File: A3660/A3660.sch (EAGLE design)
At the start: 130 parts, among them CN100 KEL8817-200-170S-F, J400 1X3PIN, U100 OSCILLATOR, U101 74F1803, U102 MC68040/68060, U103 DELAYLINE, U104 7407, U105 74F04, U200 74FCT373ASO, U201 74FCT374ASO, U202 74F32, U203 GAL16V8, U204 GAL22V10, U205 GAL22V10, U206 74F139, U207 GAL22V10, U208 GAL16V8, U209 GAL22V10, U211 GAL22V10, U212 74F257, U213 GAL22V10, U214 74FCT543A, U215 74FCT543A, U216 74FCT543A, U217 74FCT543A, U218 74FCT543A, U219 74FCT543A, U220 74FCT543A, U221 74FCT543A, U222 74FCT543A, U400 GAL22V10, U401 GAL16V8, U402 74FCT244A, U500 74F257

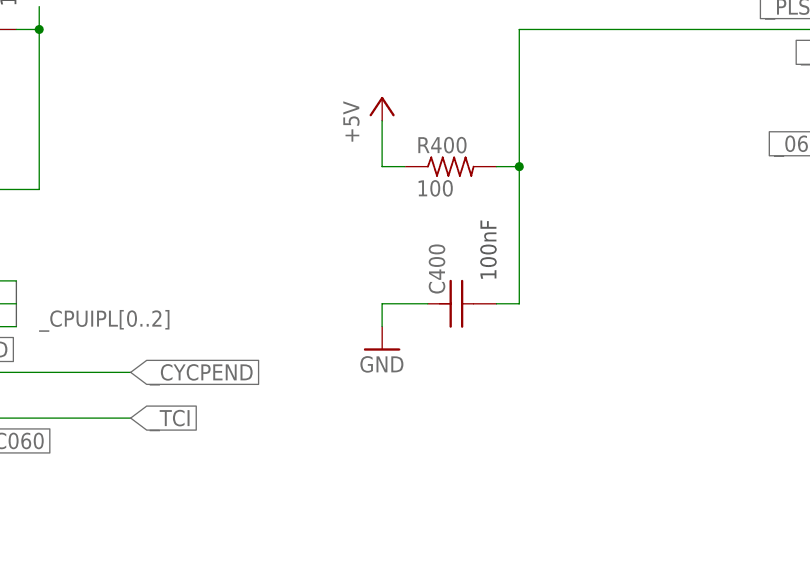
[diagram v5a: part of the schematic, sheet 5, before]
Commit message: Datalines routed,,  most addresslines aswell
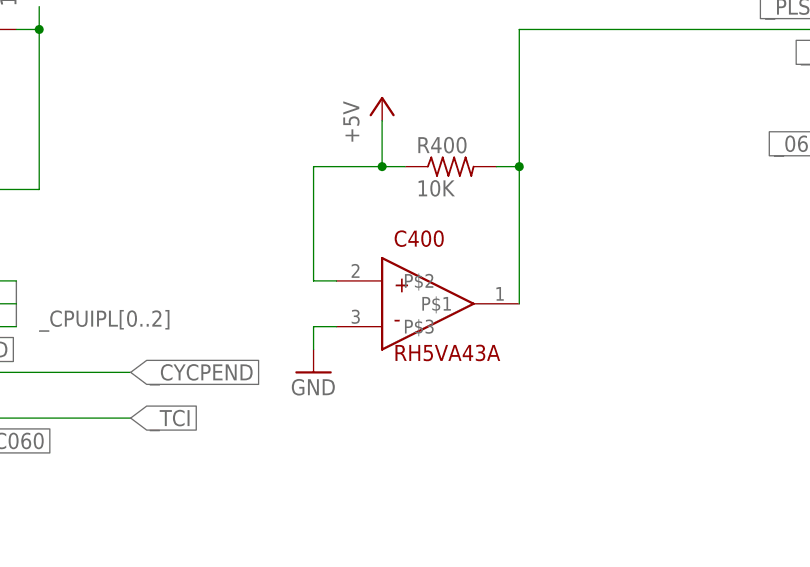
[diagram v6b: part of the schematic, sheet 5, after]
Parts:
- C400: value 100nF -> RH5VA43A; device A3660:C0805 -> A3660:RH5VA43A
- R400: value 100 -> 10K
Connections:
- net +5V: now also C400.P$2
- net GND: now also C400.P$3; no longer C400.1
- net N$1: now also C400.P$1; no longer C400.2

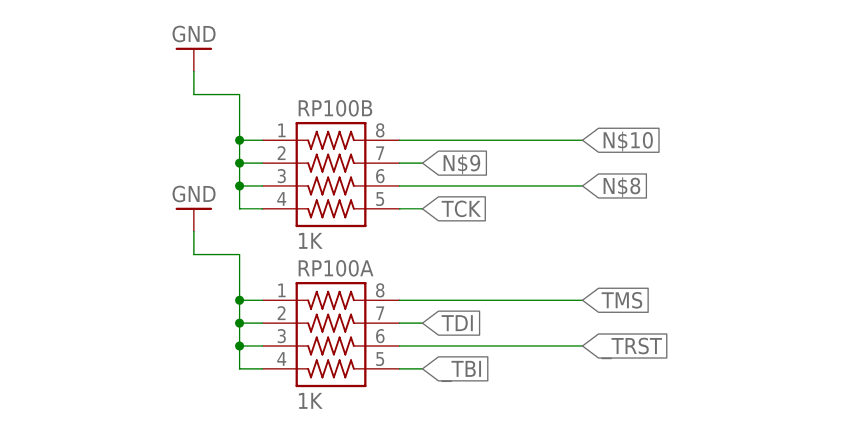
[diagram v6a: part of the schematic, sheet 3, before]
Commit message: Addresssignals complete, IPL etc working on
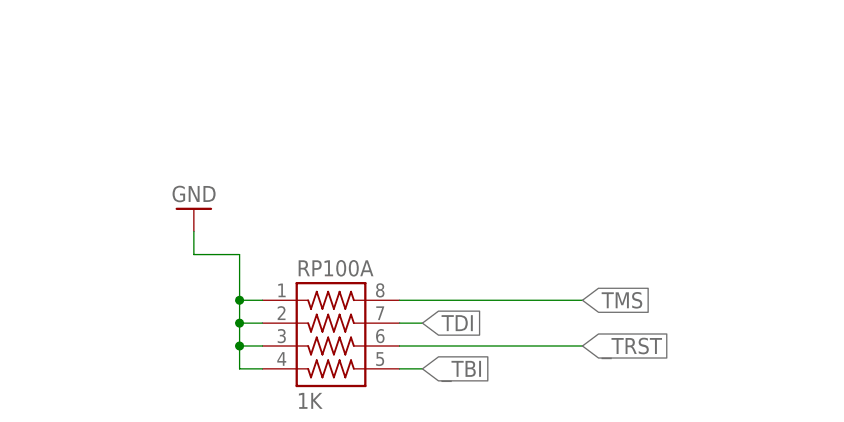
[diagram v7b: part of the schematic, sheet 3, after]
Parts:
- removed RP100B: 1K, A3660:RP743-8
- added R100A: 1k, A3660:R0805
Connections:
- removed net N$10: RP100B.8
- removed net N$8: RP100B.6
- removed net N$9: RP100B.7
- net GND: now also R100A.1; no longer RP100B.1, RP100B.2, RP100B.3, RP100B.4
- net TCK: now also R100A.2; no longer RP100B.5
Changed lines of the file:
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@@
 <part name="P+8" library="supply1" library_urn="urn:adsk.eagle:library:371" deviceset="+5V" device=""/>
 <part name="P+9" library="supply1" library_urn="urn:adsk.eagle:library:371" deviceset="+5V" device=""/>
-<part name="RP100B" library="A3660" deviceset="RP743-8" device="" value="1K"/>
 <part name="RP100A" library="A3660" deviceset="RP743-8" device="" value="1K"/>
-<part name="GND3" library="supply1" library_urn="urn:adsk.eagle:library:371" deviceset="GND" device=""/>
 <part name="GND4" library="supply1" library_urn="urn:adsk.eagle:library:371" deviceset="GND" device=""/>
 <part name="RP400B" library="A3660" deviceset="RP743-8" device="" value="1K"/>
@@
 <part name="C400" library="A3660" deviceset="RH5VA43A" device=""/>
 <part name="GND37" library="supply1" library_urn="urn:adsk.eagle:library:371" deviceset="GND" device=""/>
+<part name="R100A" library="A3660" deviceset="R0805" device="" value="1k"/>
+<part name="GND3" library="supply1" library_urn="urn:adsk.eagle:library:371" deviceset="GND" device=""/>
 </parts>
 <sheets>
@@
 <instance part="GND42" gate="1" x="-203.2" y="116.84"/>
 <instance part="P+50" gate="1" x="-203.2" y="134.62"/>
+<instance part="R100A" gate="G$1" x="-175.26" y="81.28"/>
+<instance part="GND3" gate="1" x="-185.42" y="81.28" rot="R270"/>
 </instances>
 <busses>
@@
 <pinref part="GND42" gate="1" pin="GND"/>
 </segment>
+<segment>
+<pinref part="R100A" gate="G$1" pin="1"/>
+<wire x1="-180.34" y1="81.28" x2="-182.88" y2="81.28" width="0.1524" layer="91"/>
+<pinref part="GND3" gate="1" pin="GND"/>
+</segment>
 </net>
 <net name="060D0" class="0">
@@
 </segment>
 </net>
-<net name="TCK" class="0">
-<segment>
-<pinref part="U102" gate="G$1" pin="TCK"/>
-<wire x1="-114.3" y1="81.28" x2="-134.62" y2="81.28" width="0.1524" layer="91"/>
-<label x="-134.62" y="81.28" size="1.778" layer="95" rot="R180" xref="yes"/>
-</segment>
-</net>
 <net name="_TBI" class="0">
 <segment>
@@
 </segment>
 </net>
+<net name="TCK" class="0">
+<segment>
+<pinref part="U102" gate="G$1" pin="TCK"/>
+<wire x1="-114.3" y1="81.28" x2="-170.18" y2="81.28" width="0.1524" layer="91"/>
+<pinref part="R100A" gate="G$1" pin="2"/>
+</segment>
+</net>
 </nets>
 </sheet>
@@
 <instance part="P+8" gate="1" x="53.34" y="127"/>
 <instance part="P+9" gate="1" x="53.34" y="142.24"/>
-<instance part="RP100B" gate="G$1" x="129.54" y="124.46"/>
 <instance part="RP100A" gate="G$1" x="129.54" y="106.68"/>
-<instance part="GND3" gate="1" x="114.3" y="139.7" rot="R180"/>
 <instance part="GND4" gate="1" x="114.3" y="121.92" rot="R180"/>
 <instance part="RP400B" gate="G$1" x="210.82" y="127"/>
@@
 </segment>
 </net>
-<net name="TCK" class="0">
-<segment>
-<pinref part="RP100B" gate="G$1" pin="5"/>
-<wire x1="137.16" y1="121.92" x2="139.7" y2="121.92" width="0.1524" layer="91"/>
-<label x="139.7" y="121.92" size="1.778" layer="95" xref="yes"/>
-</segment>
-</net>
-<net name="N$8" class="0">
-<segment>
-<pinref part="RP100B" gate="G$1" pin="6"/>
-<wire x1="137.16" y1="124.46" x2="157.48" y2="124.46" width="0.1524" layer="91"/>
-<label x="157.48" y="124.46" size="1.778" layer="95" xref="yes"/>
-</segment>
-</net>
-<net name="N$9" class="0">
-<segment>
-<pinref part="RP100B" gate="G$1" pin="7"/>
-<wire x1="137.16" y1="127" x2="139.7" y2="127" width="0.1524" layer="91"/>
-<label x="139.7" y="127" size="1.778" layer="95" xref="yes"/>
-</segment>
-</net>
-<net name="N$10" class="0">
-<segment>
-<pinref part="RP100B" gate="G$1" pin="8"/>
-<wire x1="137.16" y1="129.54" x2="157.48" y2="129.54" width="0.1524" layer="91"/>
-<label x="157.48" y="129.54" size="1.778" layer="95" xref="yes"/>
-</segment>
-</net>
 <net name="GND" class="0">
 <segment>
-<pinref part="RP100B" gate="G$1" pin="4"/>
-<wire x1="121.92" y1="121.92" x2="119.38" y2="121.92" width="0.1524" layer="91"/>
-<wire x1="119.38" y1="121.92" x2="119.38" y2="124.46" width="0.1524" layer="91"/>
-<wire x1="119.38" y1="124.46" x2="119.38" y2="127" width="0.1524" layer="91"/>
-<wire x1="119.38" y1="127" x2="119.38" y2="129.54" width="0.1524" layer="91"/>
-<wire x1="119.38" y1="129.54" x2="119.38" y2="134.62" width="0.1524" layer="91"/>
-<wire x1="119.38" y1="134.62" x2="114.3" y2="134.62" width="0.1524" layer="91"/>
-<wire x1="114.3" y1="134.62" x2="114.3" y2="137.16" width="0.1524" layer="91"/>
-<pinref part="GND3" gate="1" pin="GND"/>
-<pinref part="RP100B" gate="G$1" pin="3"/>
-<wire x1="121.92" y1="124.46" x2="119.38" y2="124.46" width="0.1524" layer="91"/>
-<junction x="119.38" y="124.46"/>
-<pinref part="RP100B" gate="G$1" pin="2"/>
-<wire x1="121.92" y1="127" x2="119.38" y2="127" width="0.1524" layer="91"/>
-<junction x="119.38" y="127"/>
-<pinref part="RP100B" gate="G$1" pin="1"/>
-<wire x1="121.92" y1="129.54" x2="119.38" y2="129.54" width="0.1524" layer="91"/>
-<junction x="119.38" y="129.54"/>
-</segment>
-<segment>
 <pinref part="RP100A" gate="G$1" pin="4"/>
